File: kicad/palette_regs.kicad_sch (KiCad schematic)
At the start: 3 parts, among them U113 74LS670, U115 74LS670, U136 74LS04

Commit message: More updates
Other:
- note added: "Palette Entry"
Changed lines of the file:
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@@
 		(title "Video Unit: Palette Registers")
+	)
+	(text "Palette Entry"
+		(exclude_from_sim no)
+		(at 60.96 85.852 0)
+		(effects
+			(font
+				(size 1.27 1.27)
+			)
+		)
 	)
 	(text_box "Unlike the other video registers, the Chameleon's palette registers are memory mapped. \n\nPalette register 0 is mapped at F3400-F35FFh and palette register 1 is mapped at F3600-F37FFh. Only the lower two bits are significant, so each register repeats 128 times throughout their address space. This has some interesting implications; perhaps efficient use of string instructions to set the palette.\n\nFrom the CPU perspective, these registers are write-only. The video unit addresses them wtih C0 and C1 from the graphics serializers - in essence, they replace the CGA's traditional color MUX."
@@
 		)
 	)
+	(table
+		(column_count 4)
+		(border
+			(external yes)
+			(header yes)
+			(stroke
+				(width 0)
+				(type solid)
+			)
+		)
+		(separators
+			(rows yes)
+			(cols yes)
+			(stroke
+				(width 0)
+				(type solid)
+			)
+		)
+		(column_widths 7.62 7.62 7.62 7.62)
+		(row_heights 3.81 3.81)
+		(cells
+			(table_cell "3"
+				(exclude_from_sim no)
+				(at 54.61 87.63 0)
+				(size 7.62 3.81)
+				(margins 0.9525 0.9525 0.9525 0.9525)
+				(span 1 1)
+				(fill
+					(type color)
+					(color 0 0 132 1)
+				)
+				(effects
+					(font
+						(size 1.27 1.27)
+						(color 255 255 255 1)
+					)
+				)
+			)
+			(table_cell "2"
+				(exclude_from_sim no)
+				(at 62.23 87.63 0)
+				(size 7.62 3.81)
+				(margins 0.9525 0.9525 0.9525 0.9525)
+				(span 1 1)
+				(fill
+					(type color)
+					(color 0 0 132 1)
+				)
+				(effects
+					(font
+						(size 1.27 1.27)
+						(color 255 255 255 1)
+					)
+				)
+			)
+			(table_cell "1"
+				(exclude_from_sim no)
+				(at 69.85 87.63 0)
+				(size 7.62 3.81)
+				(margins 0.9525 0.9525 0.9525 0.9525)
+				(span 1 1)
+				(fill
+					(type color)
+					(color 0 0 132 1)
+				)
+				(effects
+					(font
+						(size 1.27 1.27)
+						(color 255 255 255 1)
+					)
+				)
+			)
+			(table_cell "0"
+				(exclude_from_sim no)
+				(at 77.47 87.63 0)
+				(size 7.62 3.81)
+				(margins 0.9525 0.9525 0.9525 0.9525)
+				(span 1 1)
+				(fill
+					(type color)
+					(color 0 0 132 1)
+				)
+				(effects
+					(font
+						(size 1.27 1.27)
+						(color 255 255 255 1)
+					)
+				)
+			)
+			(table_cell "I"
+				(exclude_from_sim no)
+				(at 54.61 91.44 0)
+				(size 7.62 3.81)
+				(margins 0.9525 0.9525 0.9525 0.9525)
+				(span 1 1)
+				(fill
+					(type none)
+				)
+				(effects
+					(font
+						(size 1.27 1.27)
+					)
+				)
+			)
+			(table_cell "R"
+				(exclude_from_sim no)
+				(at 62.23 91.44 0)
+				(size 7.62 3.81)
+				(margins 0.9525 0.9525 0.9525 0.9525)
+				(span 1 1)
+				(fill
+					(type color)
+					(color 255 0 0 0.15)
+				)
+				(effects
+					(font
+						(size 1.27 1.27)
+					)
+				)
+			)
+			(table_cell "G"
+				(exclude_from_sim no)
+				(at 69.85 91.44 0)
+				(size 7.62 3.81)
+				(margins 0.9525 0.9525 0.9525 0.9525)
+				(span 1 1)
+				(fill
+					(type color)
+					(color 0 194 0 0.15)
+				)
+				(effects
+					(font
+						(size 1.27 1.27)
+					)
+				)
+			)
+			(table_cell "B"
+				(exclude_from_sim no)
+				(at 77.47 91.44 0)
+				(size 7.62 3.81)
+				(margins 0.9525 0.9525 0.9525 0.9525)
+				(span 1 1)
+				(fill
+					(type color)
+					(color 0 0 194 0.15)
+				)
+				(effects
+					(font
+						(size 1.27 1.27)
+					)
+				)
+			)
+		)
+	)

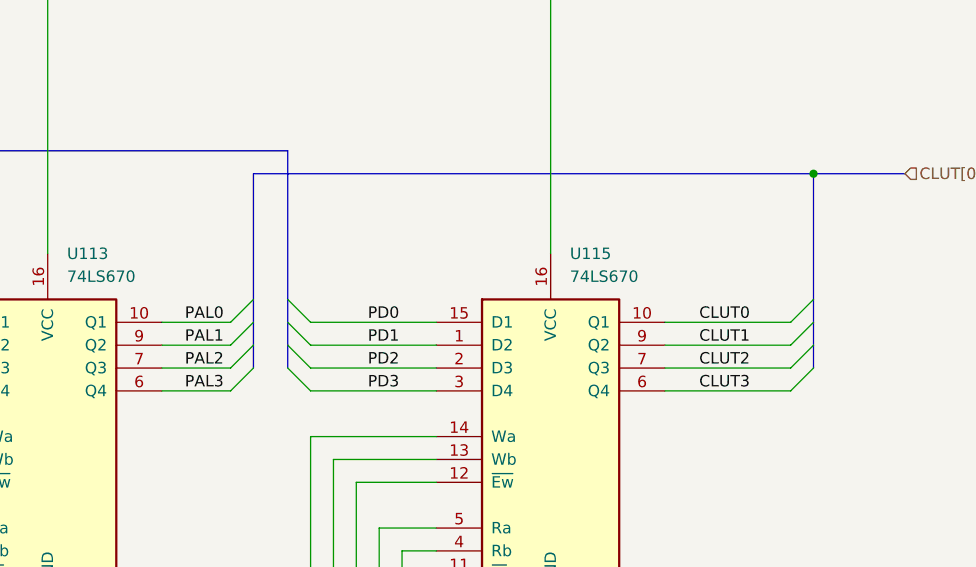
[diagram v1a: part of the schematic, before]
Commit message: Add parallel port, game port
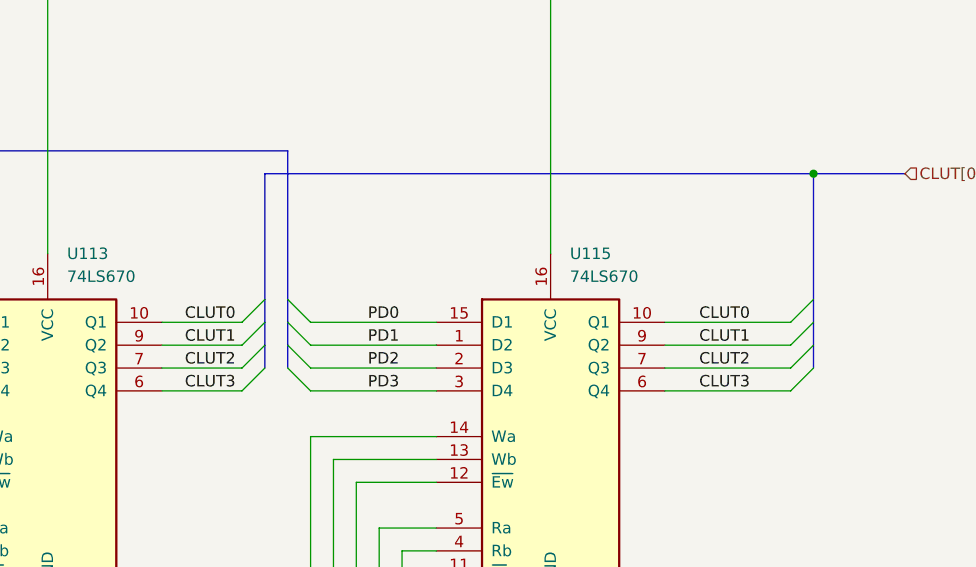
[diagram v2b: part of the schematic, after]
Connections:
- net PAL0 is gone; now on net CLUT0: U113.10 (Q1)
- net PAL1 is gone; now on net CLUT1: U113.9 (Q2)
- net PAL2 is gone; now on net CLUT2: U113.7 (Q3)
- net PAL3 is gone; now on net CLUT3: U113.6 (Q4)
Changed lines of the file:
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@@
 	)
 	(bus_entry
-		(at 154.94 90.17)
+		(at 156.21 90.17)
 		(size -2.54 2.54)
 		(stroke
@@
 	)
 	(bus_entry
-		(at 154.94 92.71)
+		(at 156.21 92.71)
 		(size -2.54 2.54)
 		(stroke
@@
 	)
 	(bus_entry
-		(at 154.94 87.63)
+		(at 156.21 87.63)
 		(size -2.54 2.54)
 		(stroke
@@
 	)
 	(bus_entry
-		(at 154.94 95.25)
+		(at 156.21 95.25)
 		(size -2.54 2.54)
 		(stroke
@@
 	(wire
 		(pts
-			(xy 144.78 95.25) (xy 152.4 95.25)
+			(xy 144.78 95.25) (xy 153.67 95.25)
 		)
 		(stroke
@@
 	(bus
 		(pts
-			(xy 154.94 95.25) (xy 154.94 92.71)
+			(xy 156.21 95.25) (xy 156.21 92.71)
 		)
 		(stroke
@@
 	(wire
 		(pts
-			(xy 144.78 97.79) (xy 152.4 97.79)
+			(xy 144.78 97.79) (xy 153.67 97.79)
 		)
 		(stroke
@@
 	(bus
 		(pts
-			(xy 154.94 87.63) (xy 154.94 73.66)
+			(xy 156.21 87.63) (xy 156.21 73.66)
 		)
 		(stroke
@@
 	(bus
 		(pts
-			(xy 154.94 73.66) (xy 217.17 73.66)
+			(xy 156.21 73.66) (xy 217.17 73.66)
 		)
 		(stroke
@@
 	(wire
 		(pts
-			(xy 144.78 90.17) (xy 152.4 90.17)
+			(xy 144.78 90.17) (xy 153.67 90.17)
 		)
 		(stroke
@@
 	(bus
 		(pts
-			(xy 154.94 92.71) (xy 154.94 90.17)
+			(xy 156.21 92.71) (xy 156.21 90.17)
 		)
 		(stroke
@@
 	(wire
 		(pts
-			(xy 144.78 92.71) (xy 152.4 92.71)
-		)
-		(stroke
-			(width 0)
-			(type default)
-		)
-	)
-	(bus
-		(pts
-			(xy 154.94 90.17) (xy 154.94 87.63)
+			(xy 144.78 92.71) (xy 153.67 92.71)
+		)
+		(stroke
+			(width 0)
+			(type default)
+		)
+	)
+	(bus
+		(pts
+			(xy 156.21 90.17) (xy 156.21 87.63)
 		)
 		(stroke
@@
 		)
 	)
+	(label "CLUT3"
+		(at 147.32 97.79 0)
+		(effects
+			(font
+				(size 1.27 1.27)
+			)
+			(justify left bottom)
+		)
+	)
 	(label "PD0"
 		(at 109.22 90.17 0)
@@
 		)
 	)
-	(label "PAL1"
-		(at 147.32 92.71 0)
-		(effects
-			(font
-				(size 1.27 1.27)
-			)
-			(justify left bottom)
-		)
-	)
 	(label "CLUT1"
 		(at 204.47 92.71 0)
@@
 		)
 	)
+	(label "CLUT2"
+		(at 147.32 95.25 0)
+		(effects
+			(font
+				(size 1.27 1.27)
+			)
+			(justify left bottom)
+		)
+	)
+	(label "CLUT1"
+		(at 147.32 92.71 0)
+		(effects
+			(font
+				(size 1.27 1.27)
+			)
+			(justify left bottom)
+		)
+	)
 	(label "PD1"
 		(at 167.64 92.71 0)
@@
 		)
 	)
-	(label "PAL3"
-		(at 147.32 97.79 0)
-		(effects
-			(font
-				(size 1.27 1.27)
-			)
-			(justify left bottom)
-		)
-	)
-	(label "PAL2"
-		(at 147.32 95.25 0)
-		(effects
-			(font
-				(size 1.27 1.27)
-			)
-			(justify left bottom)
-		)
-	)
 	(label "CLUT0"
 		(at 204.47 90.17 0)
@@
 		)
 	)
-	(label "PAL0"
+	(label "CLUT0"
 		(at 147.32 90.17 0)
 		(effects

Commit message: Updates, chameleon logo
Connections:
- net CLUT0 renamed C_{b}
- net CLUT1 renamed C_{g}
- net CLUT2 renamed C_{r}
- net CLUT3 renamed C_{i}
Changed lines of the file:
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@@
 		)
 	)
-	(label "CLUT2"
+	(label "C_{r}"
 		(at 204.47 95.25 0)
 		(effects
@@
 		)
 	)
-	(label "CLUT3"
+	(label "C_{i}"
 		(at 147.32 97.79 0)
 		(effects
@@
 		)
 	)
-	(label "CLUT1"
+	(label "C_{g}"
 		(at 204.47 92.71 0)
 		(effects
@@
 		)
 	)
-	(label "CLUT3"
+	(label "C_{i}"
 		(at 204.47 97.79 0)
 		(effects
@@
 		)
 	)
-	(label "CLUT2"
+	(label "C_{r}"
 		(at 147.32 95.25 0)
 		(effects
@@
 		)
 	)
-	(label "CLUT1"
+	(label "C_{g}"
 		(at 147.32 92.71 0)
 		(effects
@@
 		)
 	)
-	(label "CLUT0"
+	(label "C_{b}"
 		(at 204.47 90.17 0)
 		(effects
@@
 		)
 	)
-	(label "CLUT0"
+	(label "C_{b}"
 		(at 147.32 90.17 0)
 		(effects
@@
 		)
 	)
-	(hierarchical_label "CLUT[0..3]"
+	(hierarchical_label "{CLUT}"
 		(shape input)
 		(at 227.33 73.66 0)
